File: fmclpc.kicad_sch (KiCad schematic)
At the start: 3 parts, among them J1401 ASP-134604-01, J1402 ASP-134604-01

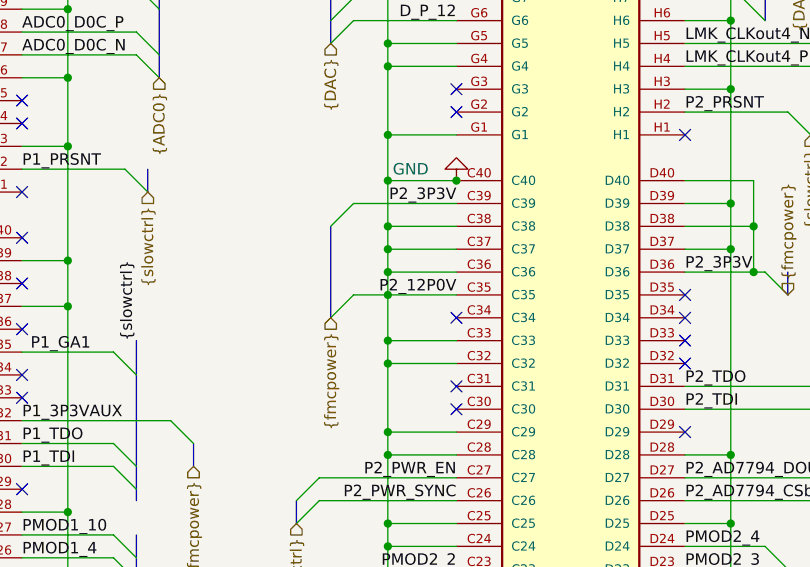
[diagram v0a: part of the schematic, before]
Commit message: J1402 C35 and C37 should not connect to the GND. It should look like the P1_12P0V side
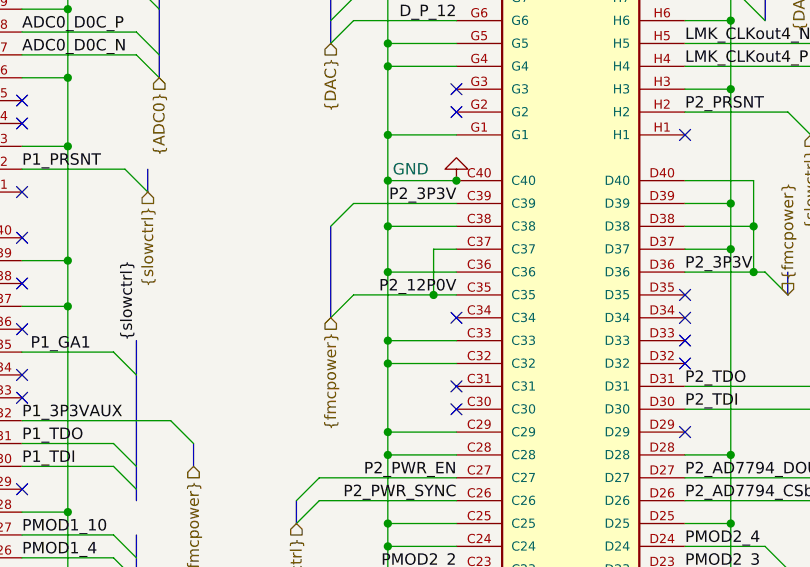
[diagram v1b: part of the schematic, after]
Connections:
- net GND: no longer J1402.C35, J1402.C37
- new net P2_12P0V: J1402.C35, J1402.C37
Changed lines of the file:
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@@
 	)
 	(junction
-		(at 124.46 148.59)
-		(diameter 0)
-		(color 0 0 0 0)
-	)
-	(junction
 		(at 124.46 176.53)
 		(diameter 0)
@@
 	)
 	(junction
-		(at 124.46 143.51)
-		(diameter 0)
-		(color 0 0 0 0)
-	)
-	(junction
 		(at 162.56 229.87)
 		(diameter 0)
@@
 	)
 	(junction
+		(at 129.54 148.59)
+		(diameter 0)
+		(color 0 0 0 0)
+	)
+	(junction
 		(at 50.8 220.98)
 		(diameter 0)
@@
 	(wire
 		(pts
-			(xy 124.46 148.59) (xy 120.65 148.59)
+			(xy 120.65 148.59) (xy 129.54 148.59)
 		)
 		(stroke
@@
 	(wire
 		(pts
-			(xy 124.46 143.51) (xy 124.46 140.97)
-		)
-		(stroke
-			(width 0)
-			(type default)
-		)
-	)
-	(wire
-		(pts
 			(xy 83.82 63.5) (xy 88.9 63.5)
 		)
@@
 	(wire
 		(pts
+			(xy 132.08 143.51) (xy 129.54 143.51)
+		)
+		(stroke
+			(width 0)
+			(type default)
+		)
+	)
+	(wire
+		(pts
 			(xy 52.07 149.86) (xy 52.07 154.94)
 		)
@@
 		)
 	)
-	(wire
-		(pts
-			(xy 132.08 143.51) (xy 124.46 143.51)
-		)
-		(stroke
-			(width 0)
-			(type default)
-		)
-	)
 	(bus
 		(pts
@@
 	(wire
 		(pts
-			(xy 132.08 148.59) (xy 124.46 148.59)
-		)
-		(stroke
-			(width 0)
-			(type default)
-		)
-	)
-	(wire
-		(pts
 			(xy 46.99 68.58) (xy 58.42 68.58)
 		)
@@
 	(wire
 		(pts
-			(xy 124.46 143.51) (xy 124.46 146.05)
+			(xy 124.46 140.97) (xy 124.46 146.05)
 		)
 		(stroke
@@
 	(wire
 		(pts
+			(xy 129.54 148.59) (xy 132.08 148.59)
+		)
+		(stroke
+			(width 0)
+			(type default)
+		)
+	)
+	(wire
+		(pts
 			(xy 124.46 234.95) (xy 132.08 234.95)
 		)
@@
 	(wire
 		(pts
-			(xy 124.46 153.67) (xy 124.46 148.59)
+			(xy 124.46 146.05) (xy 124.46 153.67)
 		)
 		(stroke
@@
 		)
 	)
+	(wire
+		(pts
+			(xy 129.54 143.51) (xy 129.54 148.59)
+		)
+		(stroke
+			(width 0)
+			(type default)
+		)
+	)
 	(bus
 		(pts
@@
 		)
 		(stroke
-			(width 0)
-			(type default)
-		)
-	)
-	(wire
-		(pts
-			(xy 124.46 148.59) (xy 124.46 146.05)
-		)
-		(stroke
